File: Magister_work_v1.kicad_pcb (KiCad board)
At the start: 4 copper layers, 80 x 80 mm, 156 parts, among them J1 USB_B_Mini, J2 Conn_01x03_Pin, J3 Conn_01x03_Pin, J4 Conn_01x02_Pin, J6 Conn_01x04_Pin, J7 Conn_01x06_Pin, J8 Conn_01x04_Pin, J9 Conn_01x02_Pin, Q1 AO3400A, SW1 SW_Push, SW10 SW_Push, SW11 SW_Push, SW12 SW_Push, SW2 SW_Push, SW3 SW_Push, SW4 SW_Push, SW5 SW_Push, SW6 SW_Push, SW7 SW_Push, SW8 SW_Push, SW9 SW_Push, U1 AMS1117-3.3, U2 SRV05-4, U3 STM32F407VETx, U4 Ai-Thinker-Ra-01, U5 AT24C256, U6 Ai-Thinker-Ra-01SH, U7 ULN2003, U8 ULN2003, Y1 X322525MQB4SI, Y2 SMD03215C2

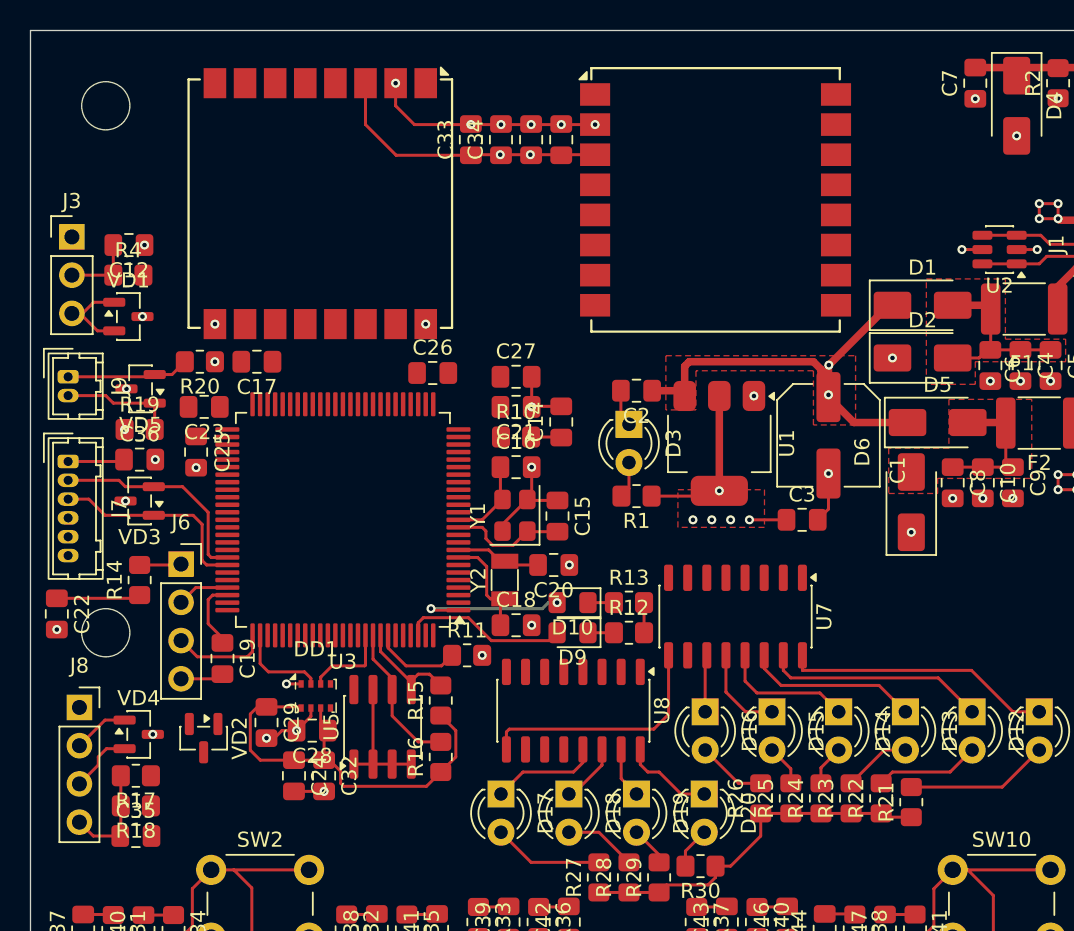
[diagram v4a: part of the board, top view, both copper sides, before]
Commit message: feat: проведены сигнальные линии ко всем UART и USB
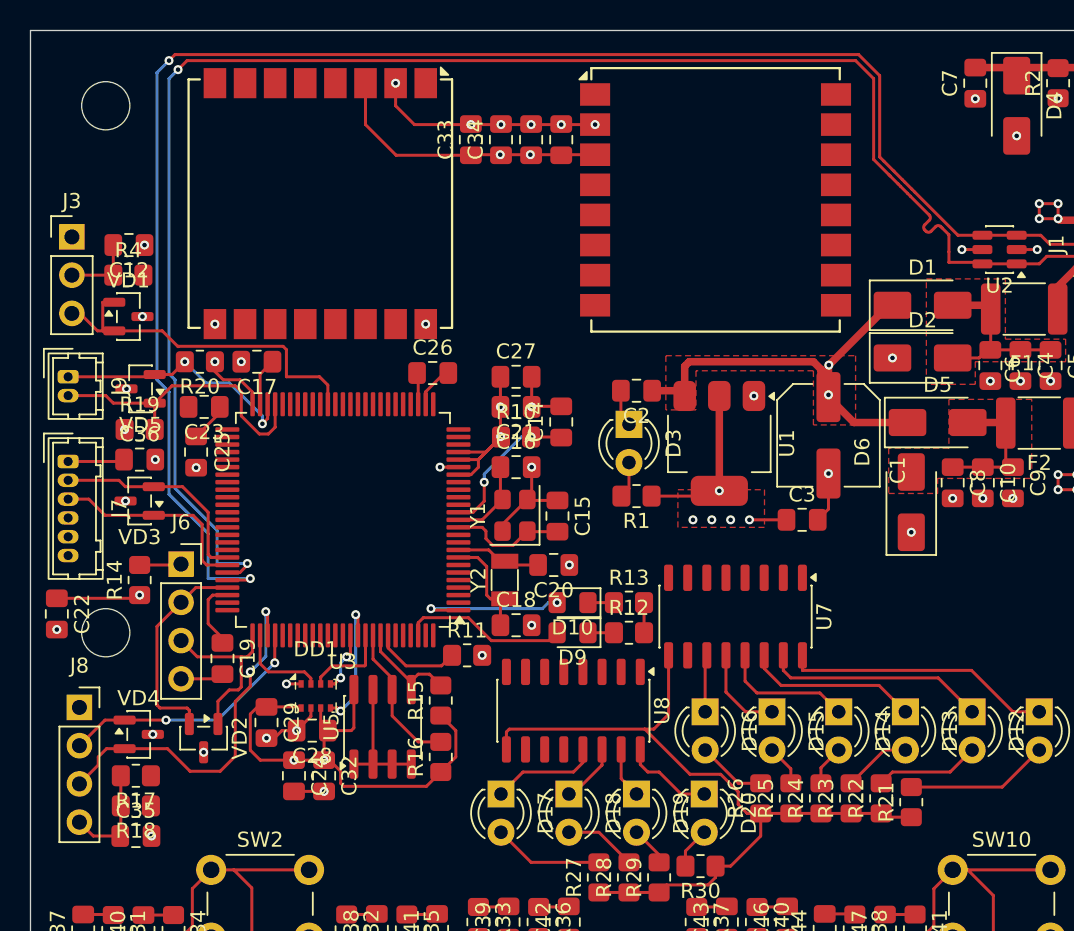
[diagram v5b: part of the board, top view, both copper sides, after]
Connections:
- U3 pad 25: DEBUG_TX1 -> unconnected-(U3-PA2-Pad25)
- U3 pad 26: DEBUG_RX1 -> unconnected-(U3-PA3-Pad26)
- U3 pad 78: UART4_TX -> DEBUG_TX1
- U3 pad 79: UART4_RX -> DEBUG_RX1
- VD2 pad 1: /STMF401_Sheet/SWDIO -> /STMF401_Sheet/SWCLK
- VD2 pad 2: /STMF401_Sheet/SWCLK -> /STMF401_Sheet/SWDIO
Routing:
- net D-: track 7.43 -> 110.3 mm, vias 0 -> 2
- net D+: track 7.47 -> 110.3 mm, vias 0 -> 2
- net +3V3: track 68.7 -> 95.7 mm, vias 9 -> 14
- net DEBUG_TX1: track 4.29 -> 24.7 mm, vias 0 -> 2
- net PWM1: track 6.41 -> 25.5 mm
- net DEBUG_RX1: track 3.70 -> 17.1 mm, vias 0 -> 2
- net BN_880_SCL: track 7.71 -> 20.2 mm
- net /STMF401_Sheet/SWDIO: track 3.48 -> 14.2 mm
- net +5V: track 75.5 -> 86.0 mm
- net SDO_BMP280: track 0.00 -> 9.01 mm, vias 0 -> 2
- net BN_880_SDA: track 8.16 -> 16.8 mm, vias 0 -> 2
- net /STMF401_Sheet/RST: track 2.02 -> 9.97 mm, vias 0 -> 2
- net /STMF401_Sheet/SWCLK: track 6.42 -> 11.9 mm
- net GND: track 80.3 -> 84.4 mm, vias 68 -> 72
- net SCK_BMP280: track 0.00 -> 3.93 mm, vias 0 -> 2
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
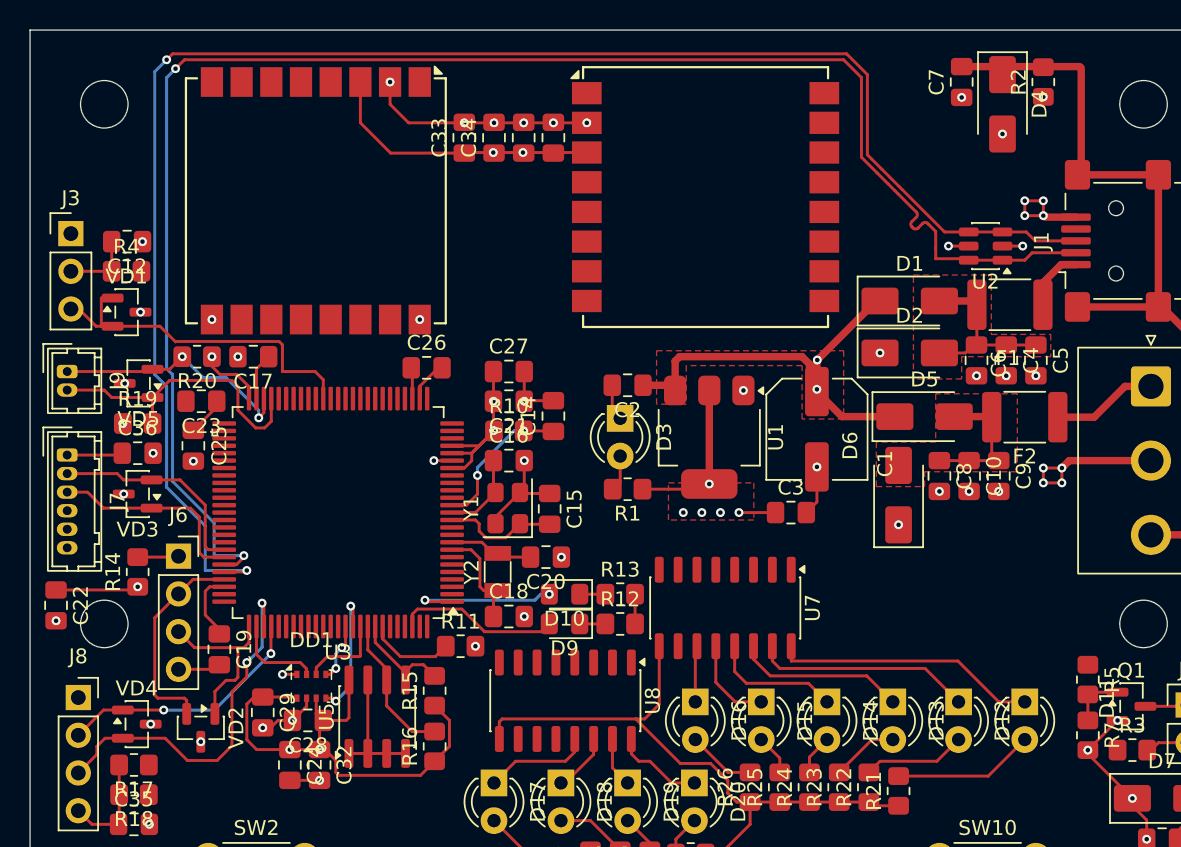
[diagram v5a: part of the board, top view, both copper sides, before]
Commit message: feat: разведены сигналньные линии для приёмо-передатчиков LoRa и LoRa_SH
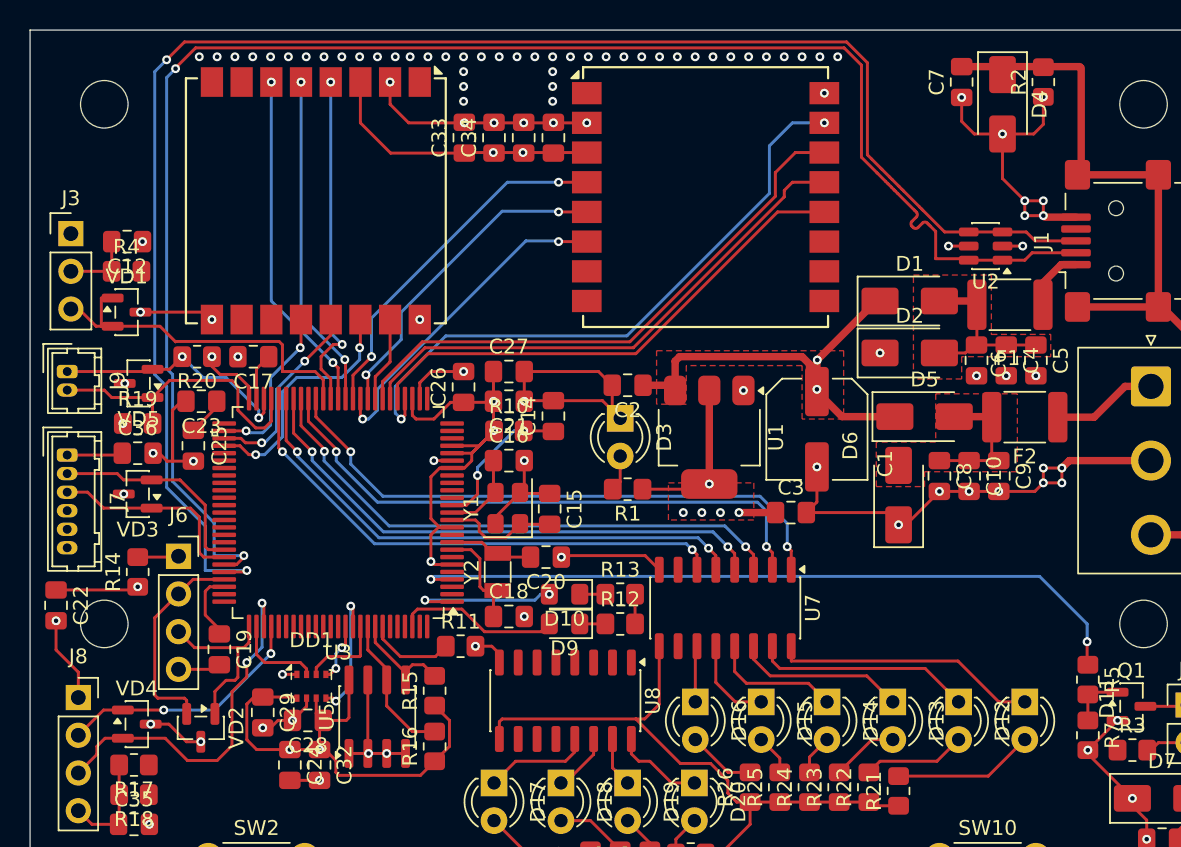
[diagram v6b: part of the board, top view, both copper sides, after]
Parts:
- moved C26 2.80 mm to (59.2, 54.0), turned to 90 degrees
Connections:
- U3 pad 5: POWER_DO1 -> unconnected-(U3-PE6-Pad5)
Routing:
- net GND: track 84.4 -> 161.1 mm, vias 72 -> 119
- net POWER_DO2: track 0.00 -> 49.8 mm, vias 0 -> 2
- net SS_LoRa: track 0.00 -> 42.0 mm, vias 0 -> 2
- net DO1: track 0.00 -> 39.7 mm, vias 0 -> 2
- net DO2: track 0.00 -> 39.5 mm, vias 0 -> 2
- net MOSI_LoRa: track 0.00 -> 38.2 mm
- net DO3: track 0.00 -> 37.4 mm, vias 0 -> 2
- net DO4: track 0.00 -> 36.8 mm, vias 0 -> 2
- net MISO_LoRa: track 0.00 -> 36.2 mm
- net DO5: track 0.00 -> 36.1 mm, vias 0 -> 2
- net DO6: track 0.00 -> 35.5 mm, vias 0 -> 2
- net SCK_LoRa: track 0.00 -> 34.5 mm
- net Reset_LoRa: track 0.00 -> 24.2 mm, vias 0 -> 2
- net DIO1_RaSH: track 0.00 -> 23.2 mm, vias 0 -> 2
- net Reset_RaSH: track 0.00 -> 22.9 mm, vias 0 -> 2
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
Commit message: feat: разведены линии DI большая часть
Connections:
- C42 pad 2: DI7 -> DI6
- C43 pad 2: DI6 -> DI7
- R36 pad 1: DI7 -> DI6
- R37 pad 1: DI6 -> DI7
- U3 pad 55: DI5 -> DI12
- U3 pad 56: DI6 -> DI11
- U3 pad 57: DI7 -> DI10
- U3 pad 58: DI8 -> DI9
- U3 pad 59: DI9 -> DI8
- U3 pad 60: DI10 -> DI7
- U3 pad 61: DI11 -> DI6
- U3 pad 62: DI12 -> DI5
- U3 pad 81: DO7 -> DO10
- U3 pad 82: DO8 -> DO9
- U3 pad 83: DO9 -> DO8
- U3 pad 84: DO10 -> DO7
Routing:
- net DI12: track 2.02 -> 79.9 mm, vias 0 -> 2
- net DI11: track 2.02 -> 47.8 mm, vias 0 -> 2
- net DI9: track 2.02 -> 47.1 mm, vias 0 -> 1
- net DI10: track 2.00 -> 46.6 mm, vias 0 -> 1
- net POWER_DO2: track 49.8 -> 7.30 mm, vias 2 -> 1
- net DI2: track 2.00 -> 29.3 mm, vias 0 -> 2
- net DI1: track 2.02 -> 27.0 mm, vias 0 -> 2
- net DI4: track 2.02 -> 27.0 mm, vias 0 -> 2
- net GND: track 161.1 -> 181.5 mm
- net DI3: track 2.02 -> 21.6 mm, vias 0 -> 2
- net DI8: track 2.02 -> 19.4 mm, vias 0 -> 1
- net DI7: track 2.02 -> 16.2 mm, vias 0 -> 1
- net +3V3: track 111.9 -> 122.7 mm
- net DI6: track 2.02 -> 4.84 mm, vias 0 -> 1
- net DI5: track 2.02 -> 4.02 mm, vias 0 -> 1

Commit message: feat: первая версия проекта,разведены все дорожки
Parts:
- moved D1 0.35 mm to (89.0, 48.0)
- moved D2 0.35 mm to (89.0, 51.5)
- moved F1 0.35 mm to (95.8, 48.2)
- moved C29 0.28 mm to (45.5, 75.8)
- moved R30 0.25 mm to (74.8, 85.5)
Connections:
- VD9 pad 3: unconnected-(VD9-A-Pad3) -> GND
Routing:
- net +5V: track 86.0 -> 249.1 mm, vias 3 -> 10
- net GND: track 181.5 -> 251.6 mm, vias 119 -> 123
- net DI7: track 16.2 -> 79.8 mm, vias 1 -> 2
- net DI8: track 19.4 -> 81.5 mm, vias 1 -> 2
- net +3V3: track 122.7 -> 172.9 mm, vias 15 -> 24
- net POWER_DO2: track 7.30 -> 55.8 mm, vias 1 -> 2
- net DI6: track 4.84 -> 41.3 mm, vias 1 -> 2
- net DI5: track 4.02 -> 39.1 mm, vias 1 -> 2
- net DI10: track 46.6 -> 78.0 mm, vias 1 -> 2
- net DO10: track 0.00 -> 31.1 mm, vias 0 -> 2
- net DI9: track 47.1 -> 78.0 mm, vias 1 -> 2
- net DI11: track 47.8 -> 78.5 mm
- net DO9: track 0.00 -> 28.6 mm, vias 0 -> 2
- net DO8: track 0.00 -> 25.5 mm, vias 0 -> 2
- net DO7: track 0.00 -> 22.7 mm, vias 0 -> 2
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- added copper zone on In2.Cu, net +3V3
- added copper zone on B.Cu, net GND
- added copper zone on F.Cu, net GND
- added copper zone on In1.Cu, net GND
- added copper zone on In2.Cu, net GND
